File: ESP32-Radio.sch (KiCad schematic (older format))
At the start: 69 parts, among them J1 BNC, J11 Conn_01x04_Female, J2 Audio_Jack, J3 Pad, J4 Pad, J6 Audio_Jack, J8 PCB_SMA, T1 6:31, T2 31:6, T3 T50_SPLITTER, T4 T50_SPLITTER, U1 LM358, U10 si5351, U11 LD33V, U2 LM358, U3 LM358, U6 MCP1703A-2502_SOT223, U7 FST3253, U8 FST3253

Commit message: added pa
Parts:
- removed C10, C7, C9: 470nF, Xenir:Capacitor 0805, symbol Xenir:Capacitor
- removed C15: .1uF, Xenir:Capacitor 0805, symbol Xenir:Capacitor
- removed C17, C18, C19, C20: 10uF, Xenir:Cap_4x5.4, symbol Xenir:Cap_Polarized
- removed C28: .1uF, Xenir:Capacitor 1206, symbol Xenir:Capacitor
- removed J1: BNC, Xenir:BNC, symbol Xenir:BNC
- removed J2: Audio_Jack, Xenir:Audio_Jack, symbol Xenir:Audio_Jack
- removed J3, J4: Pad, Xenir:Pad, symbol Xenir:Pad
- removed J8: PCB_SMA, Xenir:PCB SMA, symbol Xenir:PCB_SMA
- removed R10, R7, R8, R9: 100, Xenir:Resistor 0805, symbol Device:R_Small_US
- removed R23: 100, Xenir:Resistor 0805, symbol Xenir:Resistor
- removed R5, R6: 10k, Xenir:Resistor 0805, symbol Device:R_Small_US
- removed T2: 31:6, Xenir:T37 Transformer, symbol Xenir:T37_XFRM
- removed T3, T4: T50_SPLITTER, Xenir:T50 Trifilar, symbol Xenir:T50_SPLITTER
- removed U3: LM358, Xenir:SOIC8, symbol Xenir:LM358
- removed U7: FST3253, Xenir:SO16, symbol Xenir:FST3253
- removed VC1, VC2: 40pF, Xenir:trimcap, symbol Xenir:Trimcap
- added C51, C52, C53, C55, C57: .1uF, Xenir:Capacitor 0805, symbol Xenir:Capacitor
- added D1: 1N914, Diode_SMD:D_SOD-323_HandSoldering, symbol Diode:1N914
- added D2: D_Zener, Diode_THT:D_A-405_P10.16mm_Horizontal, symbol Device:D_Zener
- added J1: Jack-DC, Connector_BarrelJack:BarrelJack_Horizontal, symbol Connector:Jack-DC
- added J2: BNC, Xenir:BNC, symbol Xenir:BNC
- added L1, L2: Inductor, Xenir:T37_Inductor, symbol Xenir:Inductor
- added L3: 10T T37-6, Xenir:T37_Inductor, symbol Xenir:Inductor
- added L4: 11T T37-6, Xenir:T37_Inductor, symbol Xenir:Inductor
- added Q1: 2N3904-SMD, Package_TO_SOT_SMD:SOT-23, symbol Xenir:2N3904-SMD
- added Q2, Q3: 2SC5706, Package_TO_SOT_SMD:TO-252-2, symbol Xenir:2SC5706
- added R5, R52, R53, R56, R57: 1k, Xenir:Resistor 0805, symbol Xenir:Resistor
- added R54: 10k, Xenir:Resistor 0805, symbol Xenir:Resistor
- added R55: 10, Xenir:Resistor 0805, symbol Xenir:Resistor
- added R58, R6: 100, Xenir:Resistor 0805, symbol Xenir:Resistor
- added R59, R60: 1, Resistor_THT:R_Axial_DIN0204_L3.6mm_D1.6mm_P2.54mm_Vertical, symbol Xenir:Resistor
- C1, C2: value 1nF -> .1uF
- C3: value 150pF -> 220pF
- C4: value 5pF -> 150pF
- C5: value 10pF -> 470pF
- C6: value 150pF -> .1uF; footprint Xenir:Capacitor 1206 -> Xenir:Capacitor 0805
- C8: value 470nF -> 330pF; footprint Xenir:Capacitor 0805 -> Xenir:Capacitor 1206
- T1: value 6:31 -> T37_XFRM
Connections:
- net +12V: now also C6.1, C53.1, J1.1, L1.1, L2.1, R56.2, R57.1
- net +5V: now also Q1.3 (C)
- net GND: now also C3.2, C5.2, C6.2, C8.2, C53.2, C55.2, D1.1 (K), D2.2 (A), J1.2, J2.GND, R53.2, R55.2, R59.2, R6.2, R60.2; no longer C3.1, C6.1, C8.1, T1.C1A, T1.C2A
- net I_Out: now also C2.2, J6.RING, J6.RSH; no longer R2.1
- net LO_0: now also U10.2; no longer U10.0
- net LO_90: now also U10.0; no longer U10.2
- net Q_Out: now also C1.2, J6.TIP, J6.TSH; no longer R1.1
- net at T1.C1B: now also U8.9 (2A), R5.1
- net at U8.7 (1A): now also T1.C2A, R5.2
- net at R11.1, R3.2, U1.1 (OUT): now also R17.1
- net at R13.2, U1.7 (OUT): now also R18.1
- net at R12.1, R4.2, U2.1 (OUT): now also R19.1
- net at R14.2, U2.7 (OUT): now also R20.1
- removed net AudioIn: J6.RING, J6.RSH, J6.TIP, J6.TSH
- net I_OUTPUT: no longer names the net of C1.1
- net I_OUTPUT: now also R1.1
- net Q_OUTPUT: no longer names the net of C2.1
- net Q_OUTPUT: now also R2.1
- new net: C51.1, Q1.2 (E), R6.1
- new net: C51.2, Q2.1 (B), R52.2, R53.1
- new net: C52.1, R52.1, R54.2
- new net: C4.1, C52.2, L1.2, Q2.2 (C), R54.1, R56.1
- new net: Q2.3 (E), R55.1
- new net: C4.2, Q3.1 (B), R58.2
- new net: C57.1, D2.1 (K), L2.2, Q3.2 (C)
- new net: Q3.3 (E), R59.1, R60.1
- new net: C55.1, D1.2 (A), R57.2, R58.1
- new net: C8.1, J2.S (OUT), L4.2
- new net: C3.1, C57.2, L3.1
- new net: Q1.1 (B), T1.C1A, T1.C2B
- new net: C5.1, L3.2, L4.1
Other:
- moved on the sheet: C11, C12, C13, C14, C16, C21, C22, C23, C24, C25, C30, J11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

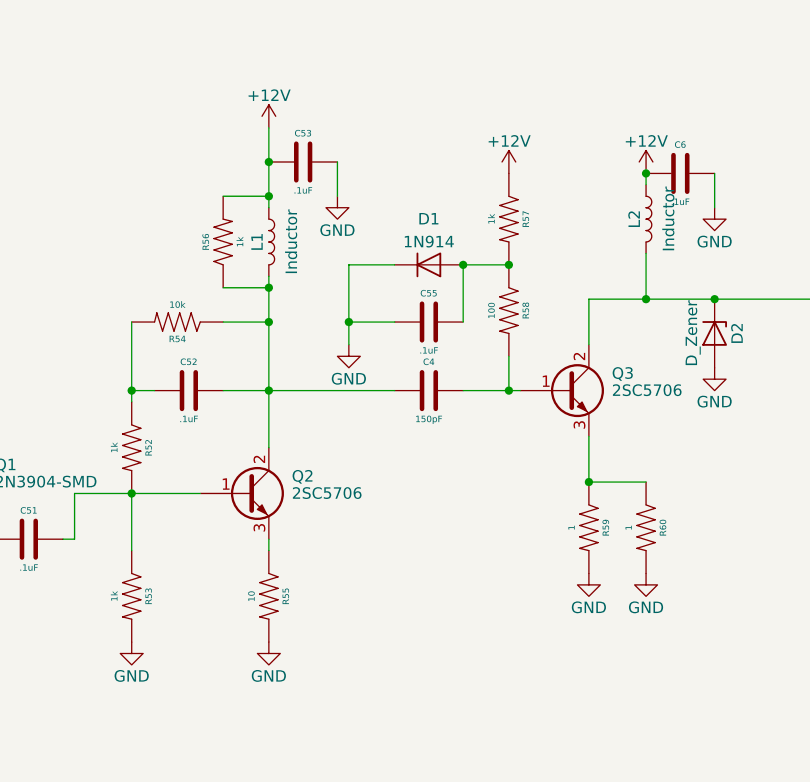
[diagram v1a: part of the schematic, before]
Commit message: added emiiter smd resistor
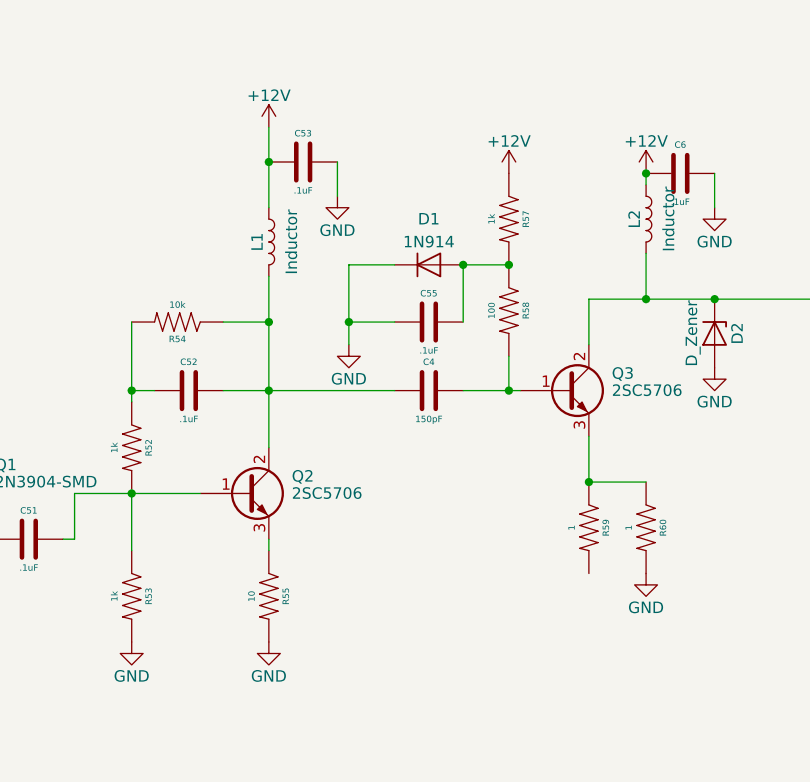
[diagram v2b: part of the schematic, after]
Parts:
- removed R56: 1k, Xenir:Resistor 0805, symbol Xenir:Resistor
- R59, R60: footprint Resistor_THT:R_Axial_DIN0204_L3.6mm_D1.6mm_P2.54mm_Vertical -> Xenir:Resistor 1206
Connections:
- net GND: no longer R59.2
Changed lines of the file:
@@
 $EndComp
-$Comp
-L Xenir:Resistor R56
-U 1 1 5F4C8BE8
-P 12150 7300
-F 0 "R56" H 12150 7375 28  0000 C CNN
-F 1 "1k" H 12150 7225 28  0000 C CNN
-F 2 "Xenir:Resistor 0805" H 12150 7200 50  0001 C CNN
-F 3 "" H 12150 7200 50  0001 C CNN
-	1    12150 7300
-	0    -1   -1   0
-$EndComp
-Wire Wire Line
-	12150 7500 12350 7500
-Connection ~ 12350 7500
-Wire Wire Line
-	12350 7500 12350 7450
-Wire Wire Line
-	12150 7100 12350 7100
-Wire Wire Line
-	12350 7100 12350 7150
 $Comp
 L power:+12V #PWR0106
@@
 Wire Wire Line
 	12350 6800 12350 6950
-Connection ~ 12350 7100
 Connection ~ 12350 6950
-Wire Wire Line
-	12350 6950 12350 7100
 Wire Wire Line
 	12650 6950 12650 7100
@@
 F 0 "R59" H 13750 8625 28  0000 C CNN
 F 1 "1" H 13750 8475 28  0000 C CNN
-F 2 "Resistor_THT:R_Axial_DIN0204_L3.6mm_D1.6mm_P2.54mm_Vertical" H 13750 8450 50  0001 C CNN
+F 2 "Xenir:Resistor 1206" H 13750 8450 50  0001 C CNN
 F 3 "" H 13750 8450 50  0001 C CNN
 	1    13750 8550
@@
 F 0 "R60" H 14000 8625 28  0000 C CNN
 F 1 "1" H 14000 8475 28  0000 C CNN
-F 2 "Resistor_THT:R_Axial_DIN0204_L3.6mm_D1.6mm_P2.54mm_Vertical" H 14000 8450 50  0001 C CNN
+F 2 "Xenir:Resistor 1206" H 14000 8450 50  0001 C CNN
 F 3 "" H 14000 8450 50  0001 C CNN
 	1    14000 8550
@@
 	13750 8350 14000 8350
 Connection ~ 13750 8350
-$Comp
-L power:GND #PWR0110
-U 1 1 5F4E2F56
-P 13750 8750
-F 0 "#PWR0110" H 13750 8500 50  0001 C CNN
-F 1 "GND" H 13750 8600 50  0000 C CNN
-F 2 "" H 13750 8750 50  0001 C CNN
-F 3 "" H 13750 8750 50  0001 C CNN
-	1    13750 8750
-	1    0    0    -1
-$EndComp
 $Comp
 L power:GND #PWR0111
@@
 Connection ~ 16900 7550
 Wire Wire Line
-	12350 7500 12350 7650
-Wire Wire Line
 	12150 7650 12350 7650
 Connection ~ 12350 7650
@@
 Wire Wire Line
 	12350 8650 12350 8600
+Wire Wire Line
+	12350 6950 12350 7150
+Wire Wire Line
+	12350 7450 12350 7650
 $EndSCHEMATC
